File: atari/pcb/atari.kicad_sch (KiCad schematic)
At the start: 155 parts, among them U2 Nice_Nano_V2

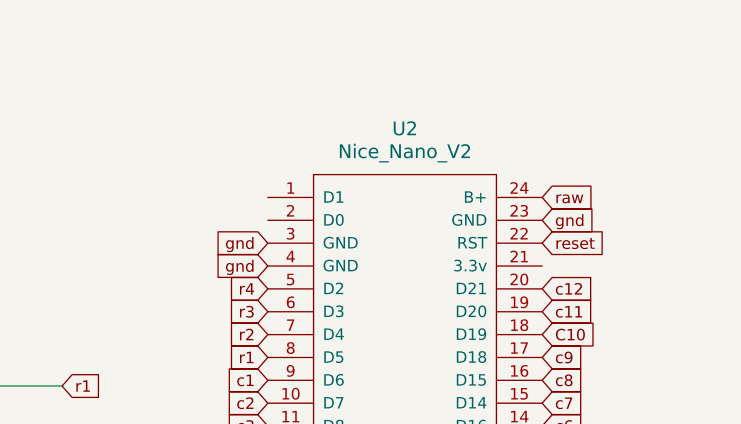
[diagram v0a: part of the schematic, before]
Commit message: moved diodes in; cleanup; fixed fill
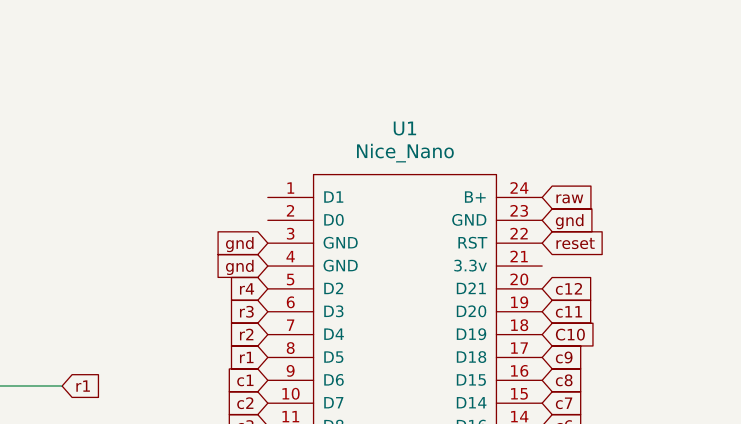
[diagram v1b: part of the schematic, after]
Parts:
- Bat+1, BatGND1, PowSw1, PowSw2: footprint Connector_Wire:SolderWire-1sqmm_1x01_D1.4mm_OD2.7mm -> Connector_Wire:SolderWire-0.5sqmm_1x01_D0.9mm_OD2.1mm
- U1: renamed from U2; value Nice_Nano_V2 -> Nice_Nano
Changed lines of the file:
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@@
       (effects (font (size 1.27 1.27)) (justify left))
     )
-    (property "Footprint" "Connector_Wire:SolderWire-1sqmm_1x01_D1.4mm_OD2.7mm" (at 262.89 130.81 0)
+    (property "Footprint" "Connector_Wire:SolderWire-0.5sqmm_1x01_D0.9mm_OD2.1mm" (at 262.89 130.81 0)
       (effects (font (size 1.27 1.27)) hide)
     )
@@
       (effects (font (size 1.27 1.27)) (justify left))
     )
-    (property "Footprint" "Connector_Wire:SolderWire-1sqmm_1x01_D1.4mm_OD2.7mm" (at 262.89 117.475 0)
+    (property "Footprint" "Connector_Wire:SolderWire-0.5sqmm_1x01_D0.9mm_OD2.1mm" (at 262.89 117.475 0)
       (effects (font (size 1.27 1.27)) hide)
     )
@@
   (symbol (lib_id "ScottoKeebs:MCU_Nice_Nano_V2") (at 250.825 41.275 0) (unit 1)
     (in_bom yes) (on_board yes) (dnp no) (fields_autoplaced)
-    (property "Reference" "U2" (at 250.825 19.685 0)
+    (property "Reference" "U1" (at 250.825 19.685 0)
       (effects (font (size 1.524 1.524)))
     )
-    (property "Value" "Nice_Nano_V2" (at 250.825 22.225 0)
+    (property "Value" "Nice_Nano" (at 250.825 22.225 0)
       (effects (font (size 1.524 1.524)))
     )
@@
       (project "atari"
         (path "/06c90a0e-9473-4f75-bdea-c580e35d9ad0"
-          (reference "U2") (unit 1)
+          (reference "U1") (unit 1)
         )
       )
@@
       (effects (font (size 1.27 1.27)) (justify left))
     )
-    (property "Footprint" "Connector_Wire:SolderWire-1sqmm_1x01_D1.4mm_OD2.7mm" (at 262.89 140.97 0)
+    (property "Footprint" "Connector_Wire:SolderWire-0.5sqmm_1x01_D0.9mm_OD2.1mm" (at 262.89 140.97 0)
       (effects (font (size 1.27 1.27)) hide)
     )
@@
       (effects (font (size 1.27 1.27)) (justify left))
     )
-    (property "Footprint" "Connector_Wire:SolderWire-1sqmm_1x01_D1.4mm_OD2.7mm" (at 262.89 107.315 0)
-      (effects (font (size 1.27 1.27)) hide)
-    )
+    (property "Footprint" "Connector_Wire:SolderWire-0.5sqmm_1x01_D0.9mm_OD2.1mm" (at 262.89 107.315 0)
+      (effects (font (size 1.27 1.27)) hide)
+    )

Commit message: added function key breakoff
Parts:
- added D5_1, D5_2, D5_3, D5_4, D5_5: Diode, ScottoKeebs_Components:Diode_DO-35, symbol ScottoKeebs:Placeholder_Diode
- added J1, J3: function_key_conn, Connector_PinHeader_2.54mm:PinHeader_1x05_P2.54mm_Vertical, symbol Connector:Conn_01x05_Pin
- added J2, J4: Conn_01x01_Pin, Connector_PinHeader_2.54mm:PinHeader_1x01_P2.54mm_Vertical, symbol Connector:Conn_01x01_Pin
- added S5_1help1, S5_2start1, S5_3select1, S5_4option1, S5_5reset1: 1u, ScottoKeebs_MX:MX_PCB_1.00u, symbol ScottoKeebs:Placeholder_Keyswitch
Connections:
- net c4: now also J1.1 (Pin_1)
- net c5: now also J1.2 (Pin_2)
- net c6: now also J1.3 (Pin_3)
- net c7: now also J1.4 (Pin_4)
- net c8: now also J1.5 (Pin_5)
- net r5: now reaches U1.2 (D0)
- net r5: now also J2.1 (Pin_1)
- new net: J3.1 (Pin_1), S5_5reset1.2
- new net: J3.2 (Pin_2), S5_4option1.2
- new net: J3.3 (Pin_3), S5_3select1.2
- new net: J3.4 (Pin_4), S5_2start1.2
- new net: J3.5 (Pin_5), S5_1help1.2
- new net: D5_1.1 (K), D5_2.1 (K), D5_3.1 (K), D5_4.1 (K), D5_5.1 (K), J4.1 (Pin_1)
- new net: D5_4.2 (A), S5_4option1.1
- new net: D5_5.2 (A), S5_5reset1.1
- new net: D5_1.2 (A), S5_1help1.1
- new net: D5_2.2 (A), S5_2start1.1
- new net: D5_3.2 (A), S5_3select1.1

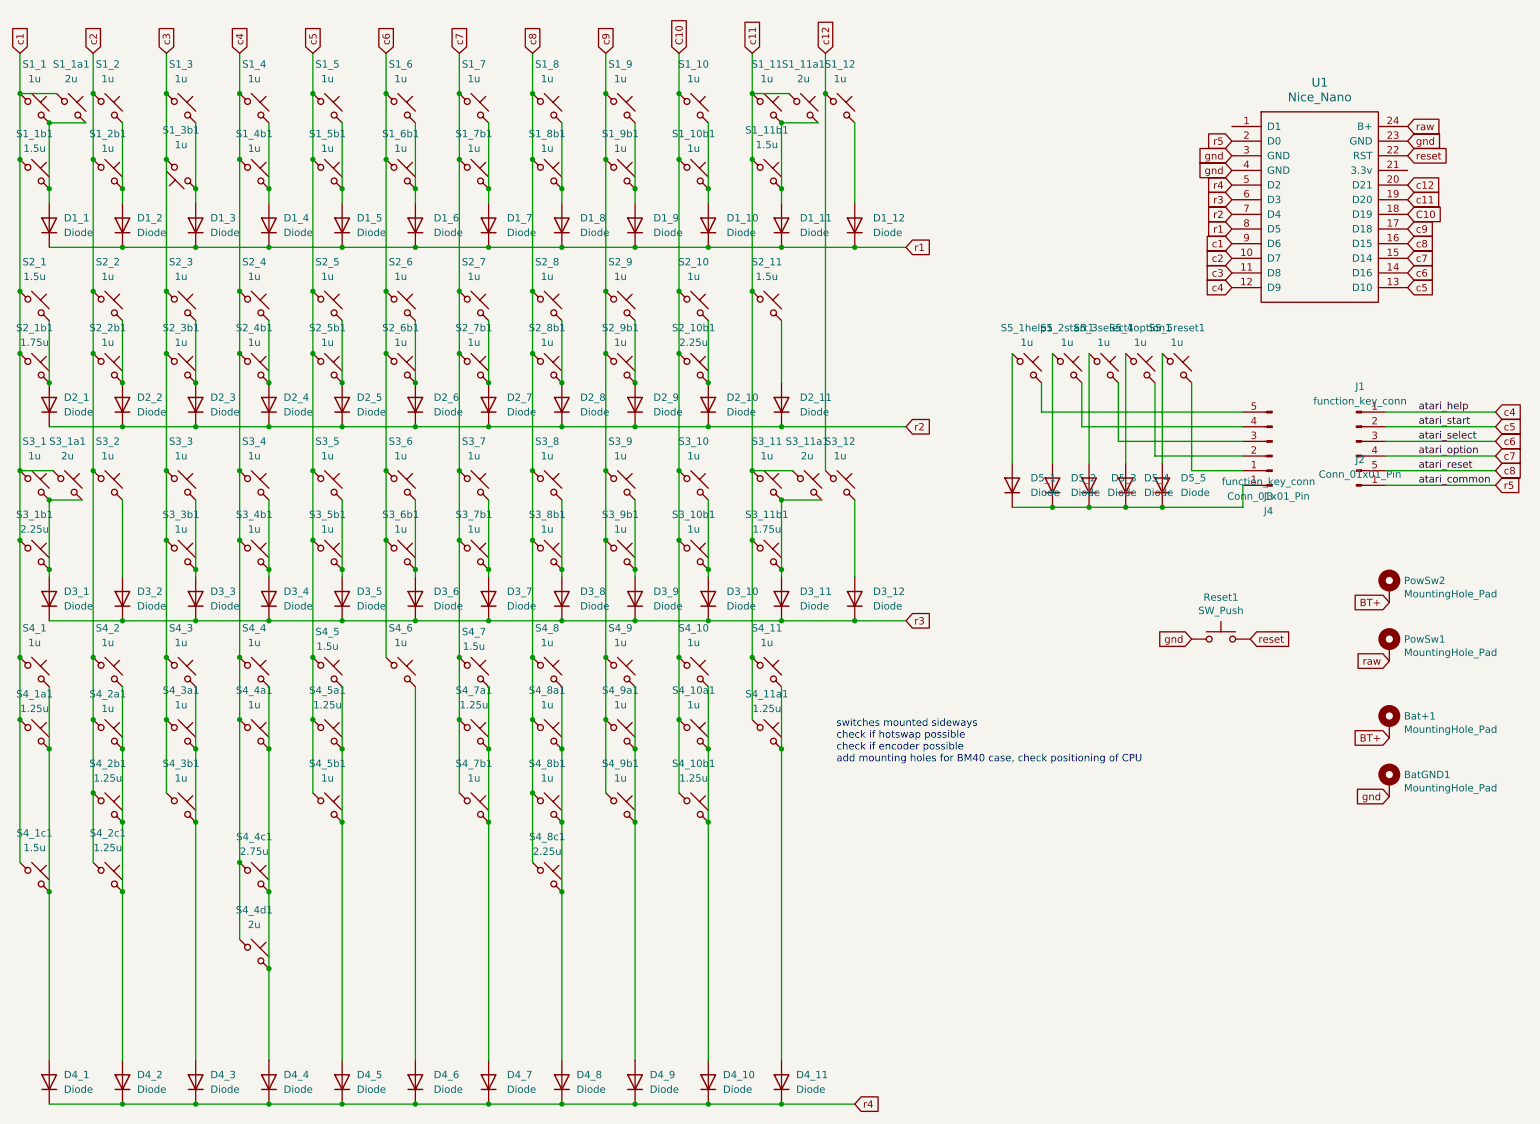
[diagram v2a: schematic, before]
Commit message: added optional encoder
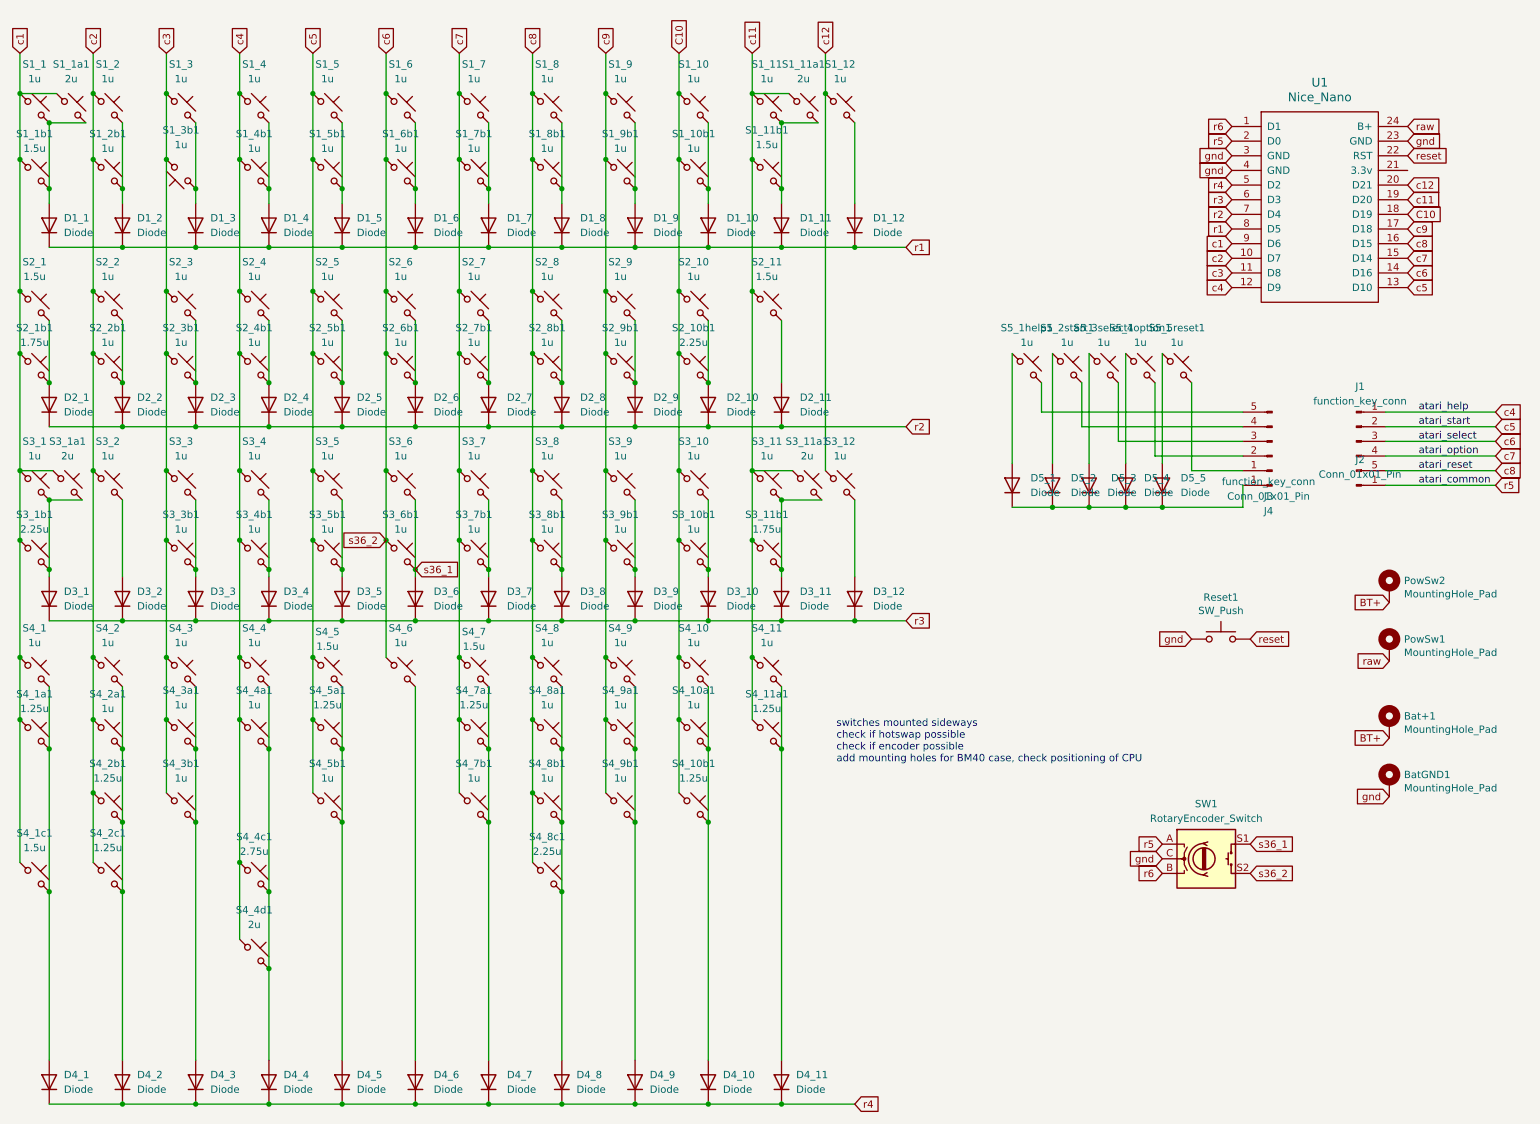
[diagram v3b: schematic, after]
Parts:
- added SW1: RotaryEncoder_Switch, Rotary_Encoder:RotaryEncoder_Alps_EC11E-Switch_Vertical_H20mm, symbol Device:RotaryEncoder_Switch
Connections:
- net c6: now also SW1.S2
- net gnd: now also SW1.C
- net r5: now also SW1.A
- net s36_1: now reaches D3_6.2 (A), S3_6.2, S3_6b1.2
- net s36_1: now also SW1.S1
- net r6: now reaches U1.1 (D1)
- net r6: now also SW1.B
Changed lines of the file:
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@@
     )
   )
+  (global_label "r6" (shape input) (at 235.585 27.305 180) (fields_autoplaced)
+    (effects (font (size 1.27 1.27)) (justify right))
+    (property "Intersheetrefs" "${INTERSHEET_REFS}" (at 230.6041 27.305 0)
+      (effects (font (size 1.27 1.27)) (justify right) hide)
+    )
+  )
   (global_label "r1" (shape input) (at 179.07 48.26 0) (fields_autoplaced)
     (effects (font (size 1.27 1.27)) (justify left))
@@
     )
   )
+  (global_label "r6" (shape input) (at 223.52 156.845 180) (fields_autoplaced)
+    (effects (font (size 1.27 1.27)) (justify right))
+    (property "Intersheetrefs" "${INTERSHEET_REFS}" (at 218.5391 156.845 0)
+      (effects (font (size 1.27 1.27)) (justify right) hide)
+    )
+  )
+  (global_label "gnd" (shape input) (at 223.52 154.305 180) (fields_autoplaced)
+    (effects (font (size 1.27 1.27)) (justify right))
+    (property "Intersheetrefs" "${INTERSHEET_REFS}" (at 217.0878 154.305 0)
+      (effects (font (size 1.27 1.27)) (justify right) hide)
+    )
+  )
   (global_label "gnd" (shape input) (at 262.89 143.51 180)
     (effects (font (size 1.27 1.27)) (justify right))
@@
     )
   )
+  (global_label "r5" (shape input) (at 223.52 151.765 180) (fields_autoplaced)
+    (effects (font (size 1.27 1.27)) (justify right))
+    (property "Intersheetrefs" "${INTERSHEET_REFS}" (at 218.5391 151.765 0)
+      (effects (font (size 1.27 1.27)) (justify right) hide)
+    )
+  )
   (global_label "c3" (shape input) (at 50.8 14.605 90) (fields_autoplaced)
     (effects (font (size 1.27 1.27)) (justify left))
@@
     )
   )
+  (global_label "s36_1" (shape input) (at 238.76 151.765 0) (fields_autoplaced)
+    (effects (font (size 1.27 1.27)) (justify left))
+    (property "Intersheetrefs" "${INTERSHEET_REFS}" (at 247.3694 151.765 0)
+      (effects (font (size 1.27 1.27)) (justify left) hide)
+    )
+  )
+  (global_label "s36_2" (shape input) (at 238.76 156.845 0) (fields_autoplaced)
+    (effects (font (size 1.27 1.27)) (justify left))
+    (property "Intersheetrefs" "${INTERSHEET_REFS}" (at 247.3694 156.845 0)
+      (effects (font (size 1.27 1.27)) (justify left) hide)
+    )
+  )
+  (global_label "s36_1" (shape input) (at 93.98 104.14 0) (fields_autoplaced)
+    (effects (font (size 1.27 1.27)) (justify left))
+    (property "Intersheetrefs" "${INTERSHEET_REFS}" (at 102.5894 104.14 0)
+      (effects (font (size 1.27 1.27)) (justify left) hide)
+    )
+  )
   (global_label "BT+" (shape input) (at 262.89 133.35 180)
     (effects (font (size 1.27 1.27)) (justify right))
@@
     )
   )
+  (global_label "s36_2" (shape input) (at 88.9 99.06 180) (fields_autoplaced)
+    (effects (font (size 1.27 1.27)) (justify right))
+    (property "Intersheetrefs" "${INTERSHEET_REFS}" (at 80.2906 99.06 0)
+      (effects (font (size 1.27 1.27)) (justify right) hide)
+    )
+  )
   (global_label "c6" (shape input) (at 266.065 52.705 0) (fields_autoplaced)
     (effects (font (size 1.27 1.27)) (justify left))
@@
         )
       )
+    )
+  )
+  (symbol (lib_id "Device:RotaryEncoder_Switch") (at 231.14 154.305 0) (unit 1)
+    (in_bom yes) (on_board yes) (dnp no) (fields_autoplaced)
+    (property "Reference" "SW1" (at 231.14 144.78 0)
+      (effects (font (size 1.27 1.27)))
+    )
+    (property "Value" "RotaryEncoder_Switch" (at 231.14 147.32 0)
+      (effects (font (size 1.27 1.27)))
+    )
+    (property "Footprint" "Rotary_Encoder:RotaryEncoder_Alps_EC11E-Switch_Vertical_H20mm" (at 227.33 150.241 0)
+      (effects (font (size 1.27 1.27)) hide)
+    )
+    (property "Datasheet" "~" (at 231.14 147.701 0)
+      (effects (font (size 1.27 1.27)) hide)
+    )
+    (pin "B")
+    (pin "C")
+    (pin "S1")
+    (pin "S2")
+    (pin "A")
+    (instances
+      (project "atari"
+        (path "/06c90a0e-9473-4f75-bdea-c580e35d9ad0"
+          (reference "SW1") (unit 1)
+        )
+      )
